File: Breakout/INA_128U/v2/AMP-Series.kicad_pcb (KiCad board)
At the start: 2 copper layers, 16.5 x 16 mm, 1 part, among them U1 INA128

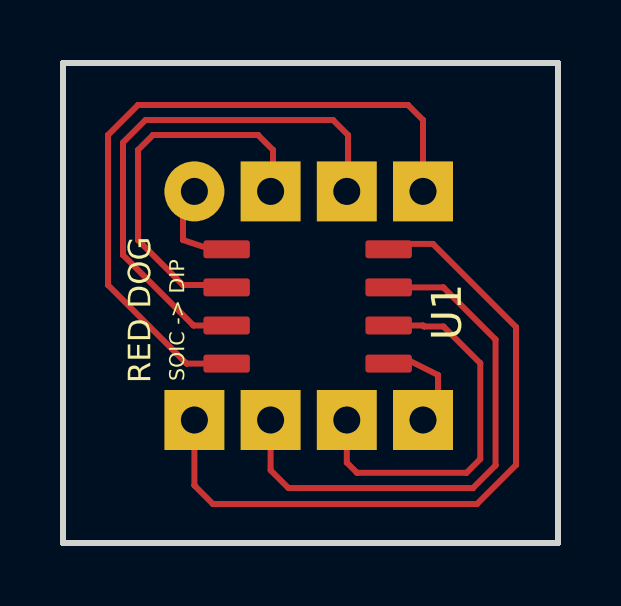
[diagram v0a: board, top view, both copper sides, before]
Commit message: added INA128_U v2
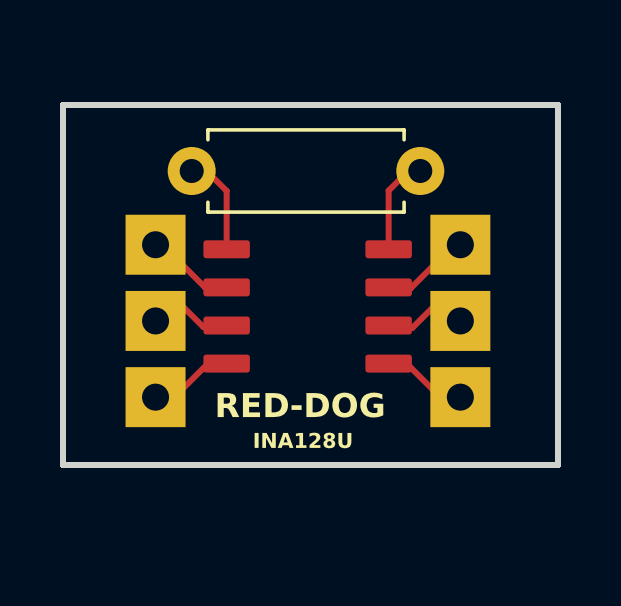
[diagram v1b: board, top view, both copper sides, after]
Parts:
- added R1: R-Gain, Resistor_THT:R_Axial_DIN0207_L6.3mm_D2.5mm_P7.62mm_Horizontal, F.Cu at (26.3, 19.2)
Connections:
- U1 pad 1: unconnected-(U1-Rg-Pad1) -> Net-(R1-Pad1)
- U1 pad 8: unconnected-(U1-Rg-Pad8) -> Net-(R1-Pad2)
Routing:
- net unconnected-(U1-Rg-Pad8): track 23.0 -> 0.00 mm
- net unconnected-(U1-V--Pad4): track 22.2 -> 2.82 mm
- net unconnected-(U1-V+-Pad7): track 18.2 -> 2.96 mm
- net unconnected-(U1-+-Pad3): track 16.8 -> 2.88 mm
- net unconnected-(U1-Pad6): track 13.0 -> 2.90 mm
- net unconnected-(U1---Pad2): track 7.21 -> 2.96 mm
- net Net-(R1-Pad1): track 0.00 -> 3.39 mm
- net Net-(R1-Pad2): track 0.00 -> 3.28 mm
- net unconnected-(U1-Ref-Pad5): track 0.00 -> 2.88 mm
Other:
- board size 16.5 x 16 mm -> 16.5 x 12 mm
- board text added: "RED-DOG"
- board text removed: "RED DOG"
- board text removed: "SOIC -> DIP"
